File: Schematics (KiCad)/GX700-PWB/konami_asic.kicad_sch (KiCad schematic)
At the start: 64 parts

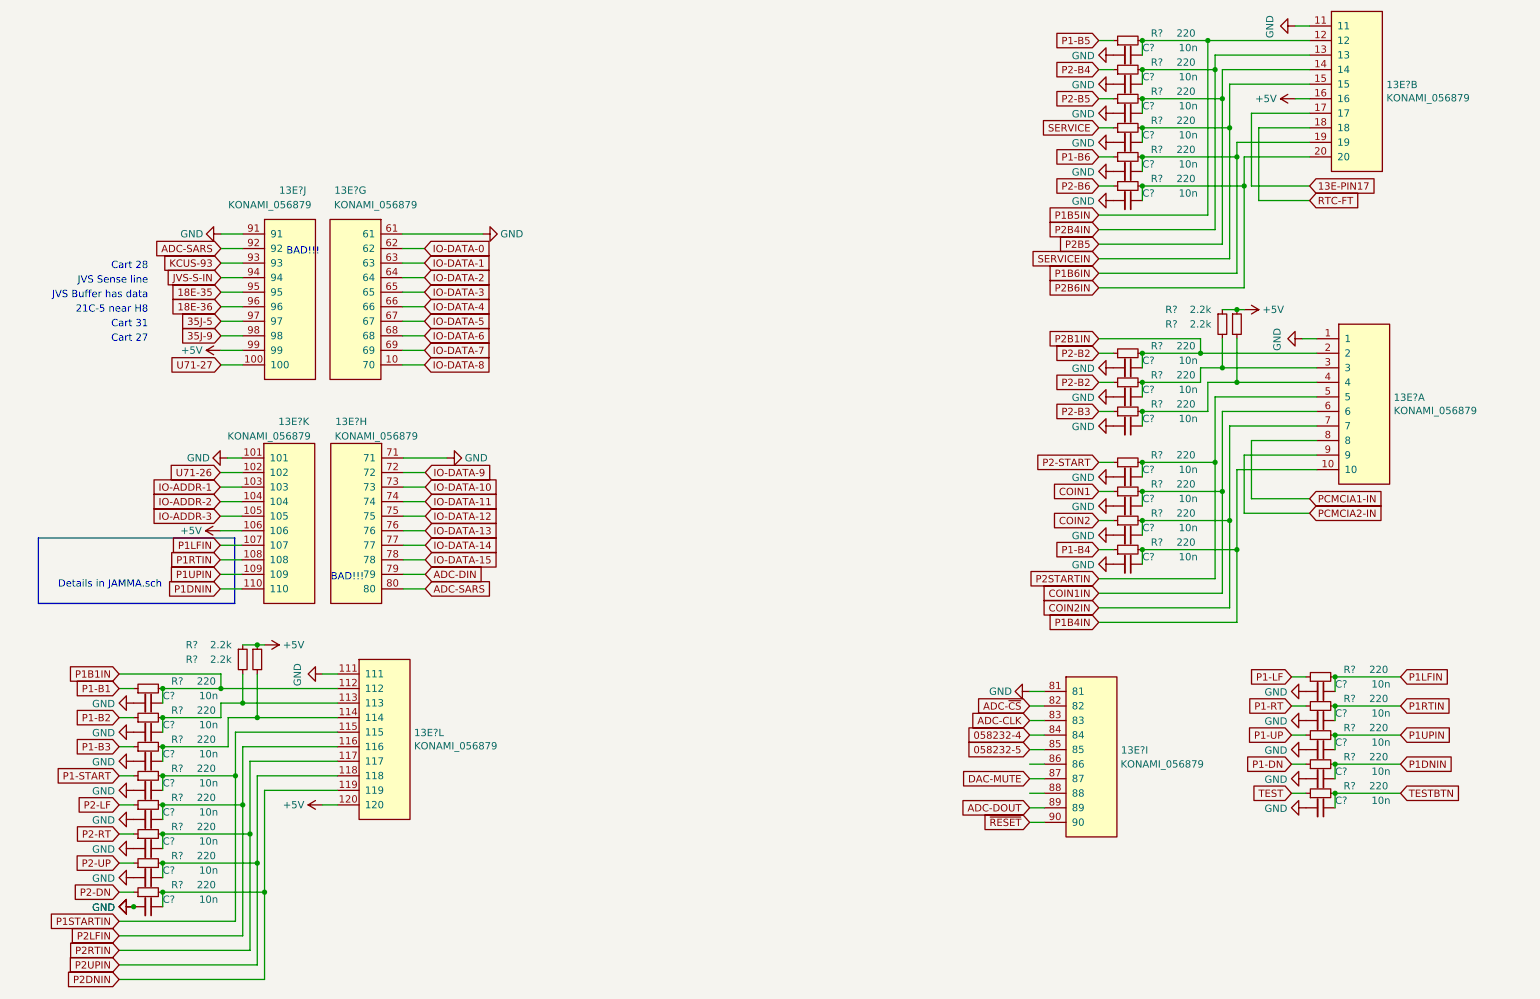
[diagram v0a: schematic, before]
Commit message: Added Symbols, PSX page
Added PSX CPU and GPU symbols, added a COH PSX skeleton schematic and also updated the JAMMA symbol and footprint as it was bad.
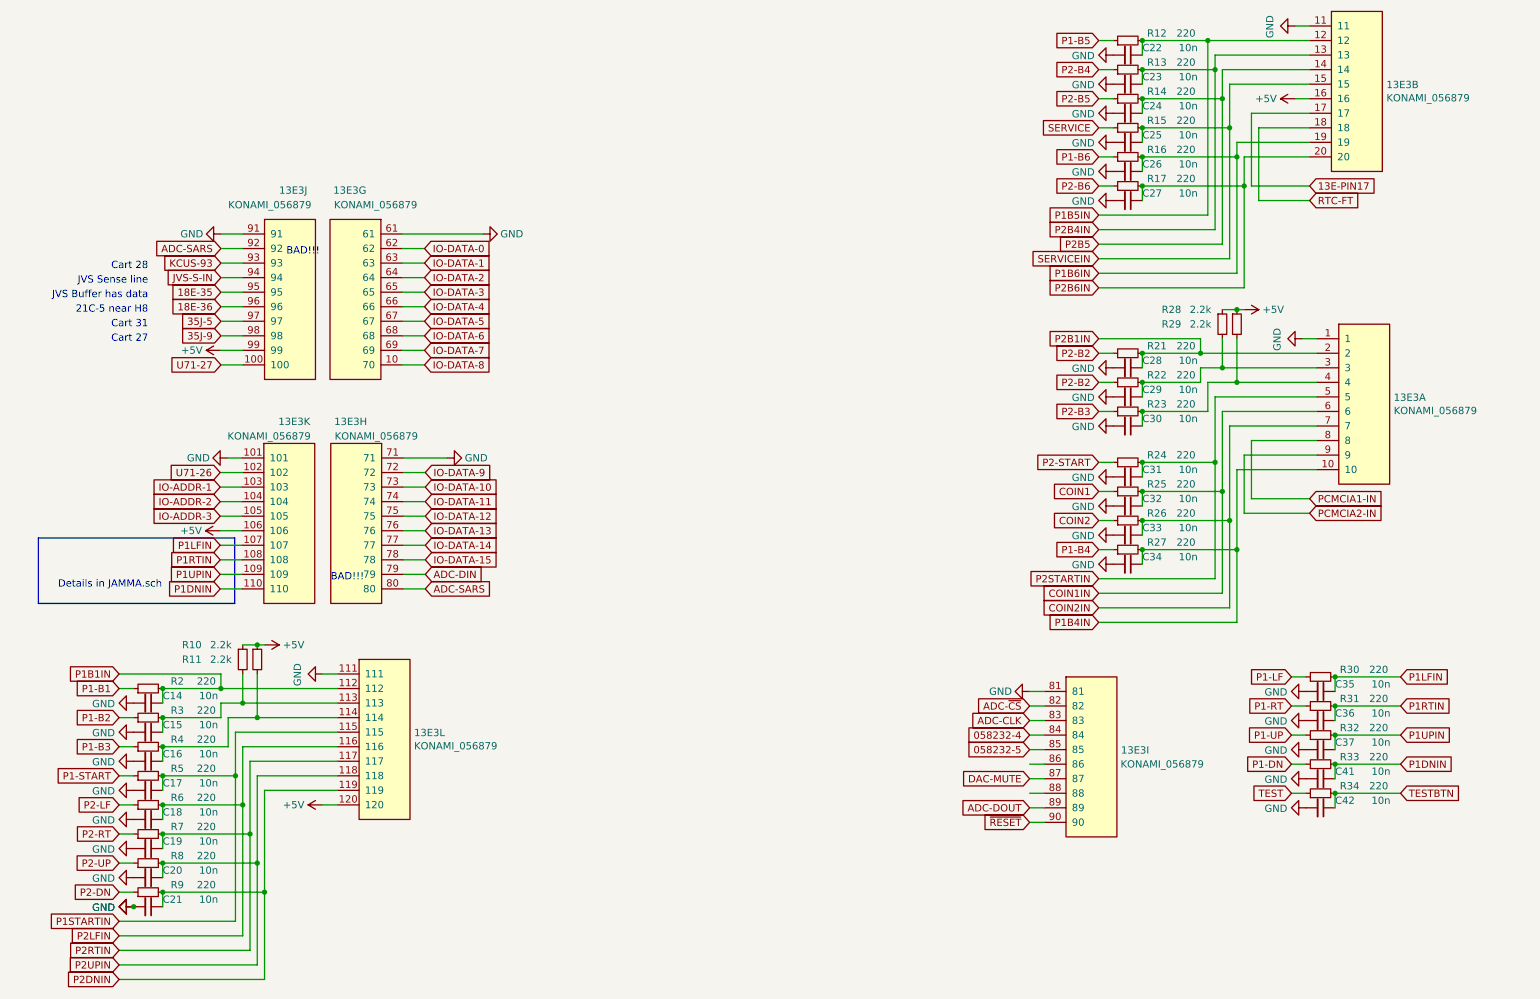
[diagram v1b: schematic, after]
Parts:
- gave numbers to parts that had none: 57

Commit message: General Fixes
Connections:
- net +5V: now also 13E3.76
- net ADC-DIN: now also 13E3.80; no longer 13E3.79
- net ADC-SARS: no longer 13E3.80
- net IO-DATA-13: now also 13E3.77; no longer 13E3.76
- net IO-DATA-14: now also 13E3.78; no longer 13E3.77
- net IO-DATA-15: now also 13E3.79; no longer 13E3.78
- net ~{AMP-MUTE}: now reaches 13E3.86
- net ~{SPU-MUTE}: now reaches 13E3.88
- net 058232-4 renamed WDC-CC2
- net 058232-5 renamed WDC-CC1
- net 18E-35 renamed H8-RX-FLAG
- net 18E-36 renamed H8-WR
- net DAC-MUTE renamed ~{CDDA-MUTE}
- net U71-26 renamed ~{KCUS-CE}
- net U71-27 renamed ~{H8-RST}
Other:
- note added: "1"
- note added: "2"
- note added: "3"
- note added: "4"
- note added: "5"
- note added: "6"
- note added: "7"
- note added: "8-Bit Output Port"
- note added: "Bus is write to H8. High until H8 clears"
- note added: "Outport - 0"
- note removed: "21C-5 near H8"
- note removed: "BAD!!!"
- moved on the sheet: 13E3A, 13E3B, 13E3G, 13E3H, 13E3I, 13E3J, 13E3K, 13E3L, C14, C15, C16, C17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

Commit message: Major board changes to give a rough render of the PCB
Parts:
- C41, C42: footprint (none) -> Capacitor_SMD:C_0805_2012Metric
- renumbered 13E3 to 13E1
